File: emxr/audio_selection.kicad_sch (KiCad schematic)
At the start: 34 parts, among them IC201 4558, J201 RCA_IN_A_B, J202 RCA_IN_3_4, J203 FRONT_AUX_IN, J204 UNKNOWN_IN, SW201 SOURCE_SELECTOR

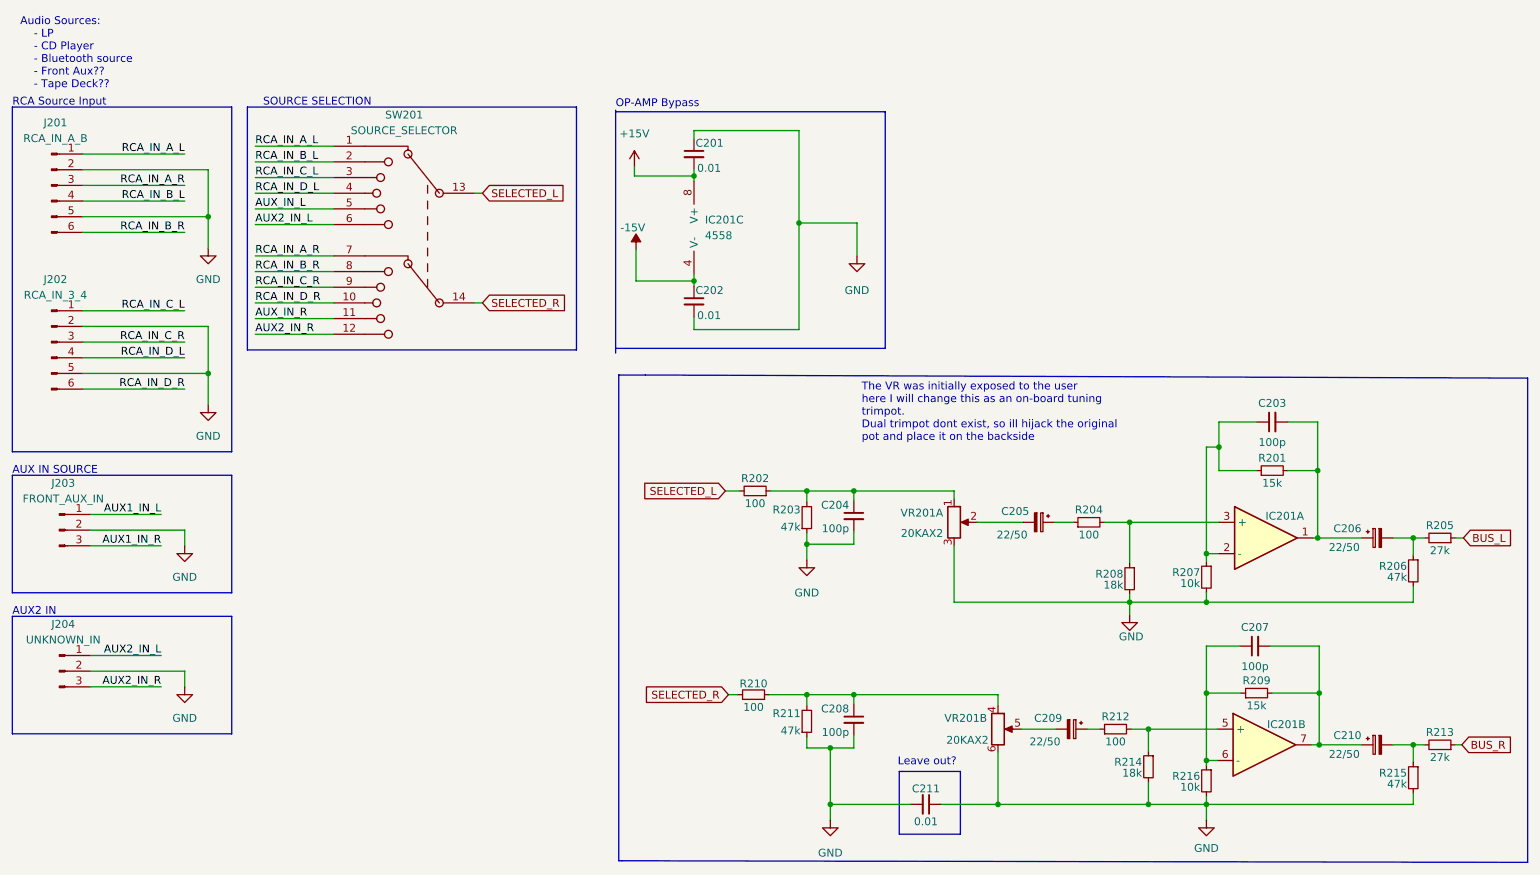
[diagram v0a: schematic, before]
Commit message: finish footprints, starting on component placement
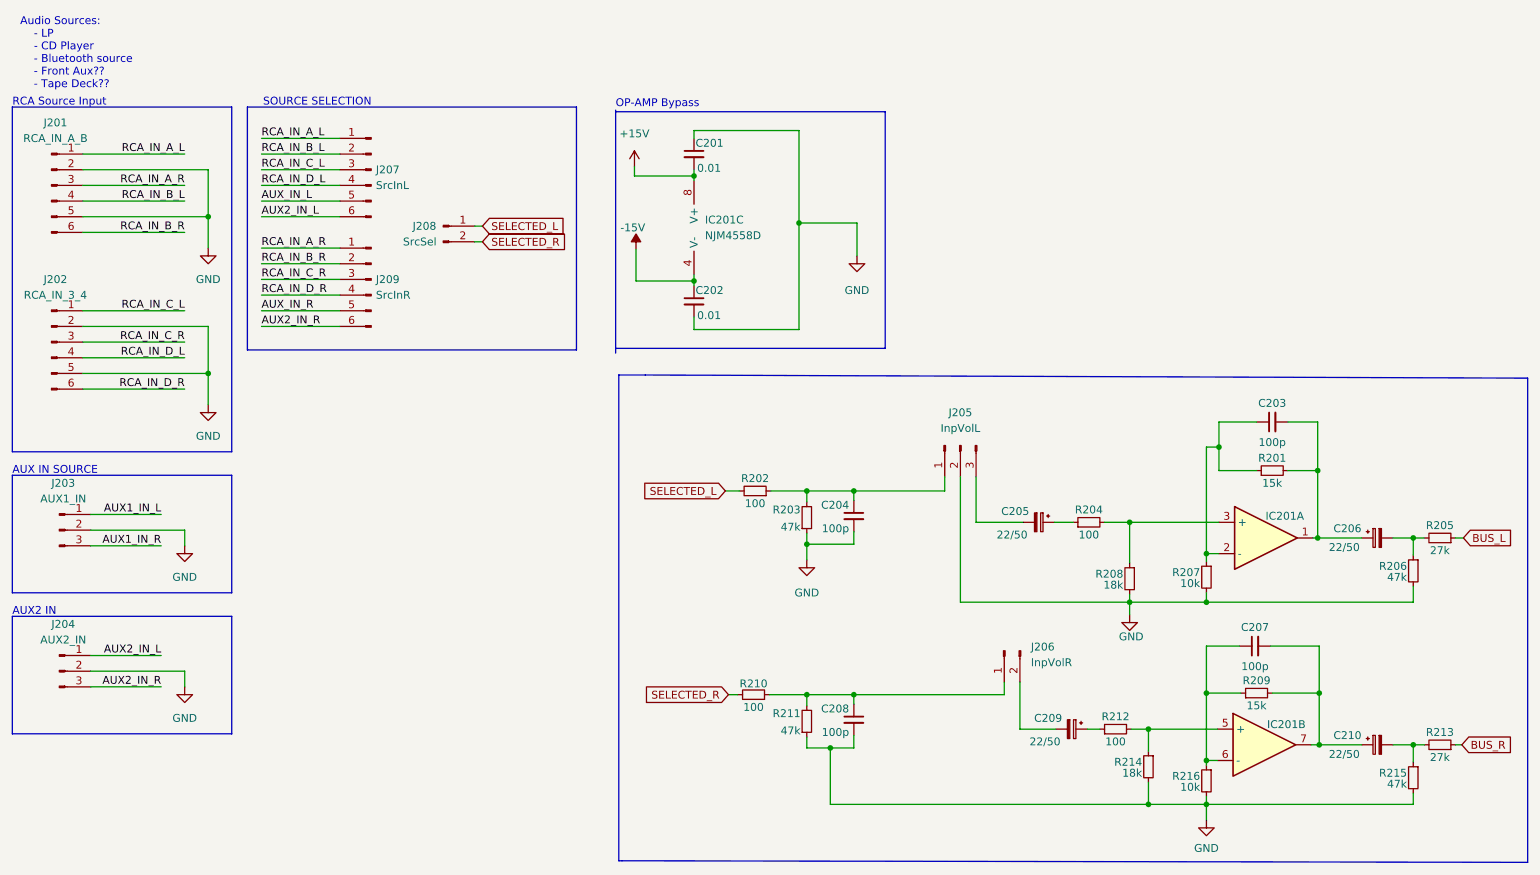
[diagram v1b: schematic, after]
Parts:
- removed C211: 0.01, symbol Device:C_Small
- removed SW201: SOURCE_SELECTOR, symbol Switch:SW_Rotary2x6
- removed VR201: 20KAX2, symbol Device:R_Potentiometer_Dual_Separate
- added J205: InpVolL, Connector_JST:JST_XH_B3B-XH-A_1x03_P2.50mm_Vertical, symbol Connector:Conn_01x03_Male
- added J206: InpVolR, Connector_JST:JST_XH_B2B-XH-A_1x02_P2.50mm_Vertical, symbol Connector:Conn_01x02_Male
- added J207: SrcInL, Connector_JST:JST_XH_B6B-XH-A_1x06_P2.50mm_Vertical, symbol Connector:Conn_01x06_Male
- added J208: SrcSel, Connector_JST:JST_XH_B2B-XH-A_1x02_P2.50mm_Vertical, symbol Connector:Conn_01x02_Male
- added J209: SrcInR, Connector_JST:JST_XH_B6B-XH-A_1x06_P2.50mm_Vertical, symbol Connector:Conn_01x06_Male
- C201, C202: footprint (none) -> Capacitor_THT:C_Disc_D3.8mm_W2.6mm_P2.50mm
- C203, C204, C207, C208: footprint (none) -> Capacitor_THT:C_Disc_D5.0mm_W2.5mm_P2.50mm
- C205, C206, C209, C210: footprint (none) -> Capacitor_THT:CP_Radial_D5.0mm_P2.00mm
- IC201: value 4558 -> NJM4558D; footprint (none) -> Package_DIP:DIP-8_W7.62mm_Socket_LongPads
- J201, J202: footprint (none) -> Connector_JST:JST_XH_B6B-XH-A_1x06_P2.50mm_Vertical
- J203: value FRONT_AUX_IN -> AUX1_IN; footprint (none) -> Connector_JST:JST_XH_B3B-XH-A_1x03_P2.50mm_Vertical
- J204: value UNKNOWN_IN -> AUX2_IN; footprint (none) -> Connector_JST:JST_XH_B3B-XH-A_1x03_P2.50mm_Vertical
- R201, R202, R203, R204, R205, R206, R207, R208, R209, R210, R211, R212, R213, R214, R215, R216: footprint (none) -> Resistor_THT:R_Axial_DIN0207_L6.3mm_D2.5mm_P10.16mm_Horizontal
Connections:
- net AUX2_IN_L: now also J207.6 (Pin_6)
- net AUX2_IN_R: now also J209.6 (Pin_6)
- net AUX_IN_L: now also J207.5 (Pin_5)
- net AUX_IN_R: now also J209.5 (Pin_5)
- net GND: now also J205.2 (Pin_2)
- net RCA_IN_A_L: now also J207.1 (Pin_1)
- net RCA_IN_A_R: now also J209.1 (Pin_1)
- net RCA_IN_B_L: now also J207.2 (Pin_2)
- net RCA_IN_B_R: now also J209.2 (Pin_2)
- net RCA_IN_C_L: now also J207.3 (Pin_3)
- net RCA_IN_C_R: now also J209.3 (Pin_3)
- net RCA_IN_D_L: now also J207.4 (Pin_4)
- net RCA_IN_D_R: now also J209.4 (Pin_4)
- net SELECTED_L: now also J208.1 (Pin_1)
- net SELECTED_R: now also J208.2 (Pin_2)
- net at C209.2: now also J206.2 (Pin_2)
- net at C205.2: now also J205.3 (Pin_3)
- net at C208.1, R210.1, R211.2: now also J206.1 (Pin_1)
- net at C204.1, R202.1, R203.2: now also J205.1 (Pin_1)
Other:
- note removed: "Leave out?"
- note removed: "The VR was initially exposed to the user here I will change this as an on-board tuning trimpot. Dual trimpot dont exist, so ill hijack the original pot and place it on the backside"

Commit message: replicated layout
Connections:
- net AUX_IN_L is gone; now on net AUX1_IN_L: J207.5 (Pin_5)
- net AUX_IN_R is gone; now on net AUX1_IN_R: J209.5 (Pin_5)
- net RCA_IN_A_R: now also J201.4 (Pin_4); no longer J201.3 (Pin_3)
- net RCA_IN_B_L: now also J201.3 (Pin_3); no longer J201.4 (Pin_4)
- net RCA_IN_C_R: now also J202.4 (Pin_4); no longer J202.3 (Pin_3)
- net RCA_IN_D_L: now also J202.3 (Pin_3); no longer J202.4 (Pin_4)
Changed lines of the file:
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@@
     (effects (font (size 1.27 1.27)) (justify left bottom))
-  )
-  (label "RCA_IN_A_R" (at 41.91 40.64 180)
-    (effects (font (size 1.27 1.27)) (justify right bottom))
   )
   (label "RCA_IN_C_L" (at 54.356 38.1 0)
@@
     (effects (font (size 1.27 1.27)) (justify left bottom))
   )
-  (label "RCA_IN_B_L" (at 41.91 43.18 180)
+  (label "RCA_IN_B_L" (at 41.91 40.64 180)
     (effects (font (size 1.27 1.27)) (justify right bottom))
   )
@@
     (effects (font (size 1.27 1.27)) (justify right bottom))
   )
-  (label "AUX_IN_R" (at 54.356 60.96 0)
+  (label "AUX1_IN_R" (at 54.356 60.96 0)
     (effects (font (size 1.27 1.27)) (justify left bottom))
   )
@@
     (effects (font (size 1.27 1.27)) (justify right bottom))
   )
+  (label "RCA_IN_D_L" (at 41.91 66.04 180)
+    (effects (font (size 1.27 1.27)) (justify right bottom))
+  )
   (label "AUX1_IN_R" (at 38.1 99.06 180)
     (effects (font (size 1.27 1.27)) (justify right bottom))
@@
     (effects (font (size 1.27 1.27)) (justify right bottom))
   )
-  (label "AUX_IN_L" (at 54.356 43.18 0)
+  (label "AUX1_IN_L" (at 54.356 43.18 0)
     (effects (font (size 1.27 1.27)) (justify left bottom))
   )
@@
   )
   (label "AUX1_IN_L" (at 38.1 93.98 180)
-    (effects (font (size 1.27 1.27)) (justify right bottom))
-  )
-  (label "RCA_IN_C_R" (at 41.91 66.04 180)
-    (effects (font (size 1.27 1.27)) (justify right bottom))
-  )
-  (label "RCA_IN_D_L" (at 41.91 68.58 180)
     (effects (font (size 1.27 1.27)) (justify right bottom))
   )
@@
     (effects (font (size 1.27 1.27)) (justify left bottom))
   )
+  (label "RCA_IN_A_R" (at 41.91 43.18 180)
+    (effects (font (size 1.27 1.27)) (justify right bottom))
+  )
   (label "AUX2_IN_L" (at 54.356 45.72 0)
     (effects (font (size 1.27 1.27)) (justify left bottom))
@@
     (effects (font (size 1.27 1.27)) (justify right bottom))
   )
+  (label "RCA_IN_C_R" (at 41.91 68.58 180)
+    (effects (font (size 1.27 1.27)) (justify right bottom))
+  )

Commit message: more routing and reshuffling
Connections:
- net at C205.2: now also J205.1 (Pin_1); no longer J205.3 (Pin_3)
- net at C204.1, R202.1, R203.2: now also J205.3 (Pin_3); no longer J205.1 (Pin_1)
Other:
- moved on the sheet: J205
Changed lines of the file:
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@@
     (pin "8")
   )
-  (symbol (lib_id "Connector:Conn_01x03_Male") (at 167.64 82.804 90) (mirror x) (unit 1)
+  (symbol (lib_id "Connector:Conn_01x03_Male") (at 167.64 82.804 270) (unit 1)
     (in_bom yes) (on_board yes) (fields_autoplaced)
     (property "Reference" "J205" (id 0) (at 167.64 77.47 90))

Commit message: first pcb draft
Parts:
- removed J201: RCA_IN_A_B, Connector_JST:JST_XH_B6B-XH-A_1x06_P2.50mm_Vertical, symbol Connector:Conn_01x06_Male
- removed J202: RCA_IN_3_4, Connector_JST:JST_XH_B6B-XH-A_1x06_P2.50mm_Vertical, symbol Connector:Conn_01x06_Male
- removed J203: AUX1_IN, Connector_JST:JST_XH_B3B-XH-A_1x03_P2.50mm_Vertical, symbol Connector:Conn_01x03_Male
- removed J204: AUX2_IN, Connector_JST:JST_XH_B3B-XH-A_1x03_P2.50mm_Vertical, symbol Connector:Conn_01x03_Male
- removed J207: SrcInL, Connector_JST:JST_XH_B6B-XH-A_1x06_P2.50mm_Vertical, symbol Connector:Conn_01x06_Male
- removed J209: SrcInR, Connector_JST:JST_XH_B6B-XH-A_1x06_P2.50mm_Vertical, symbol Connector:Conn_01x06_Male
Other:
- note removed: "AUX IN SOURCE"
- note removed: "AUX2 IN"
- note removed: "Audio Sources: - LP - CD Player - Bluetooth source - Front Aux?? - Tape Deck??"
- note removed: "RCA Source Input"
